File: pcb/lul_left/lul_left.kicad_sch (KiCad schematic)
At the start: 83 parts, among them SW1 SW_Push, SW10 SW_Push, SW11 SW_Push, SW12 SW_Push, SW13 SW_Push, SW14 SW_Push, SW15 SW_Push, SW16 SW_Push, SW17 SW_Push, SW18 SW_Push, SW19 SW_Push, SW2 SW_Push, SW20 SW_Push, SW21 SW_Push, SW22 SW_Push, SW23 SW_Push, SW24 SW_Push, SW25 SW_Push, SW26 SW_Push, SW27 SW_Push, SW28 SW_Push, SW29 SW_Push, SW3 SW_Push, SW30 SW_Push, SW31 SW_Push, SW32 SW_Push, SW33 SW_Push, SW34 SW_Push, SW35 SW_Push, SW36 SW_Push, SW37 SW_Push, SW38 SW_Push, SW39 SW_Push, SW4 SW_Push, SW40 SW_Push, SW41 SW_RESET, SW42 SW_SPDT, SW5 SW_Push, SW6 SW_Push, SW7 SW_Push, SW8 SW_Push, SW9 SW_Push, U2 nice_nano

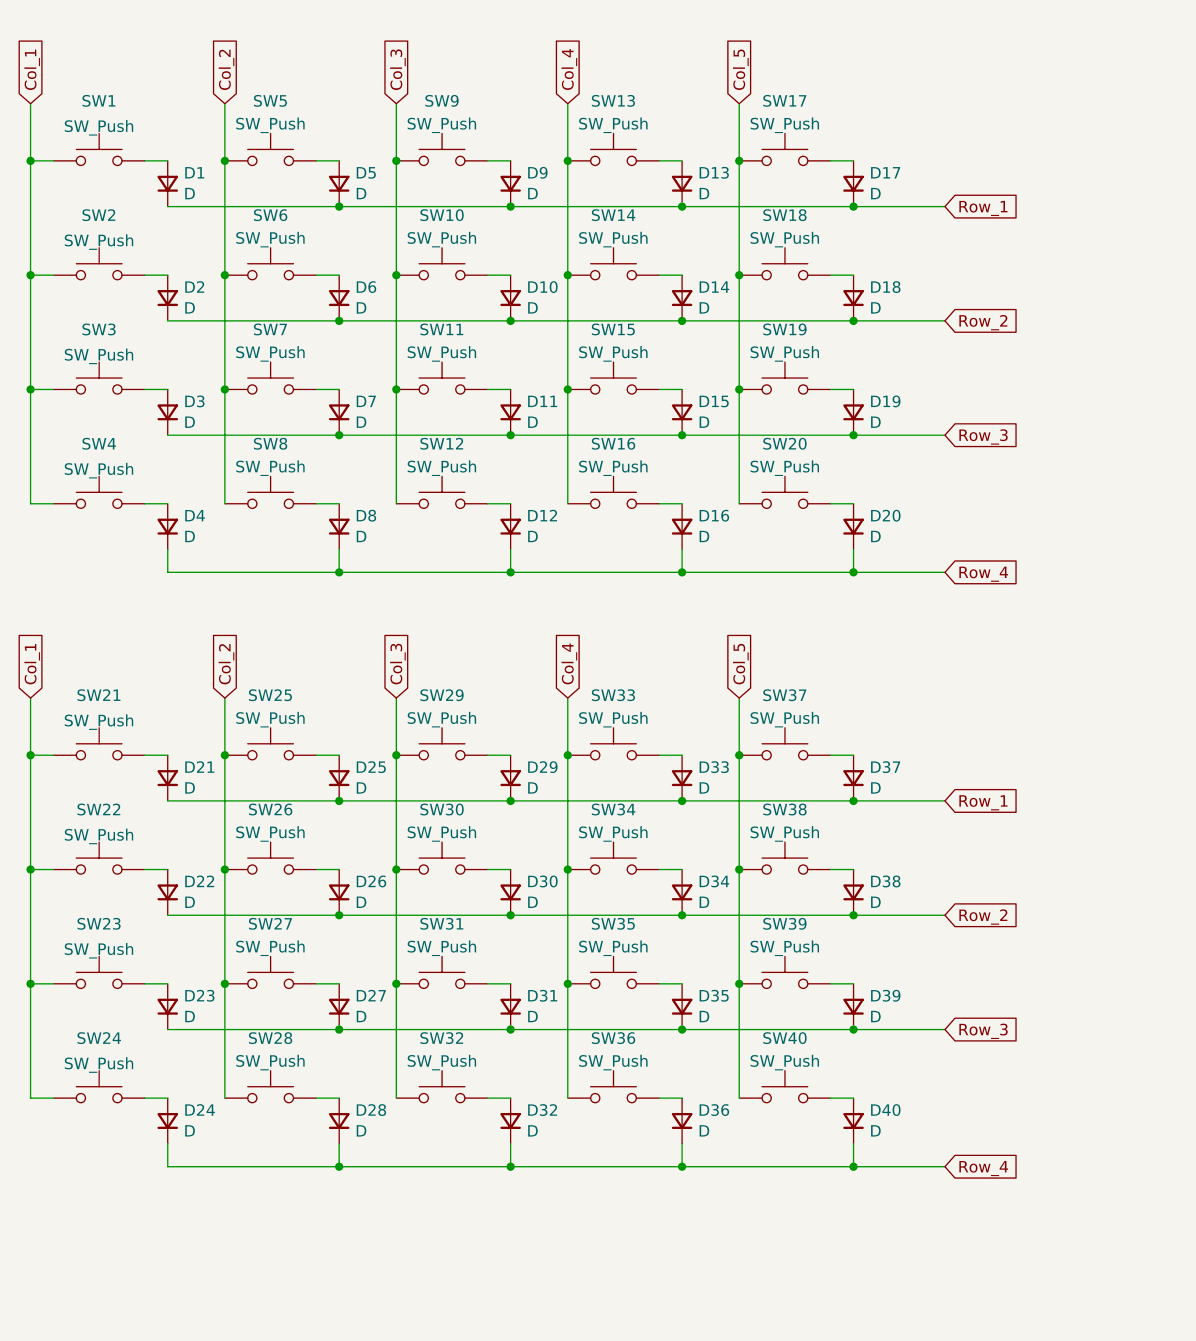
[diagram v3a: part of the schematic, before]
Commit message: Fixed switch count
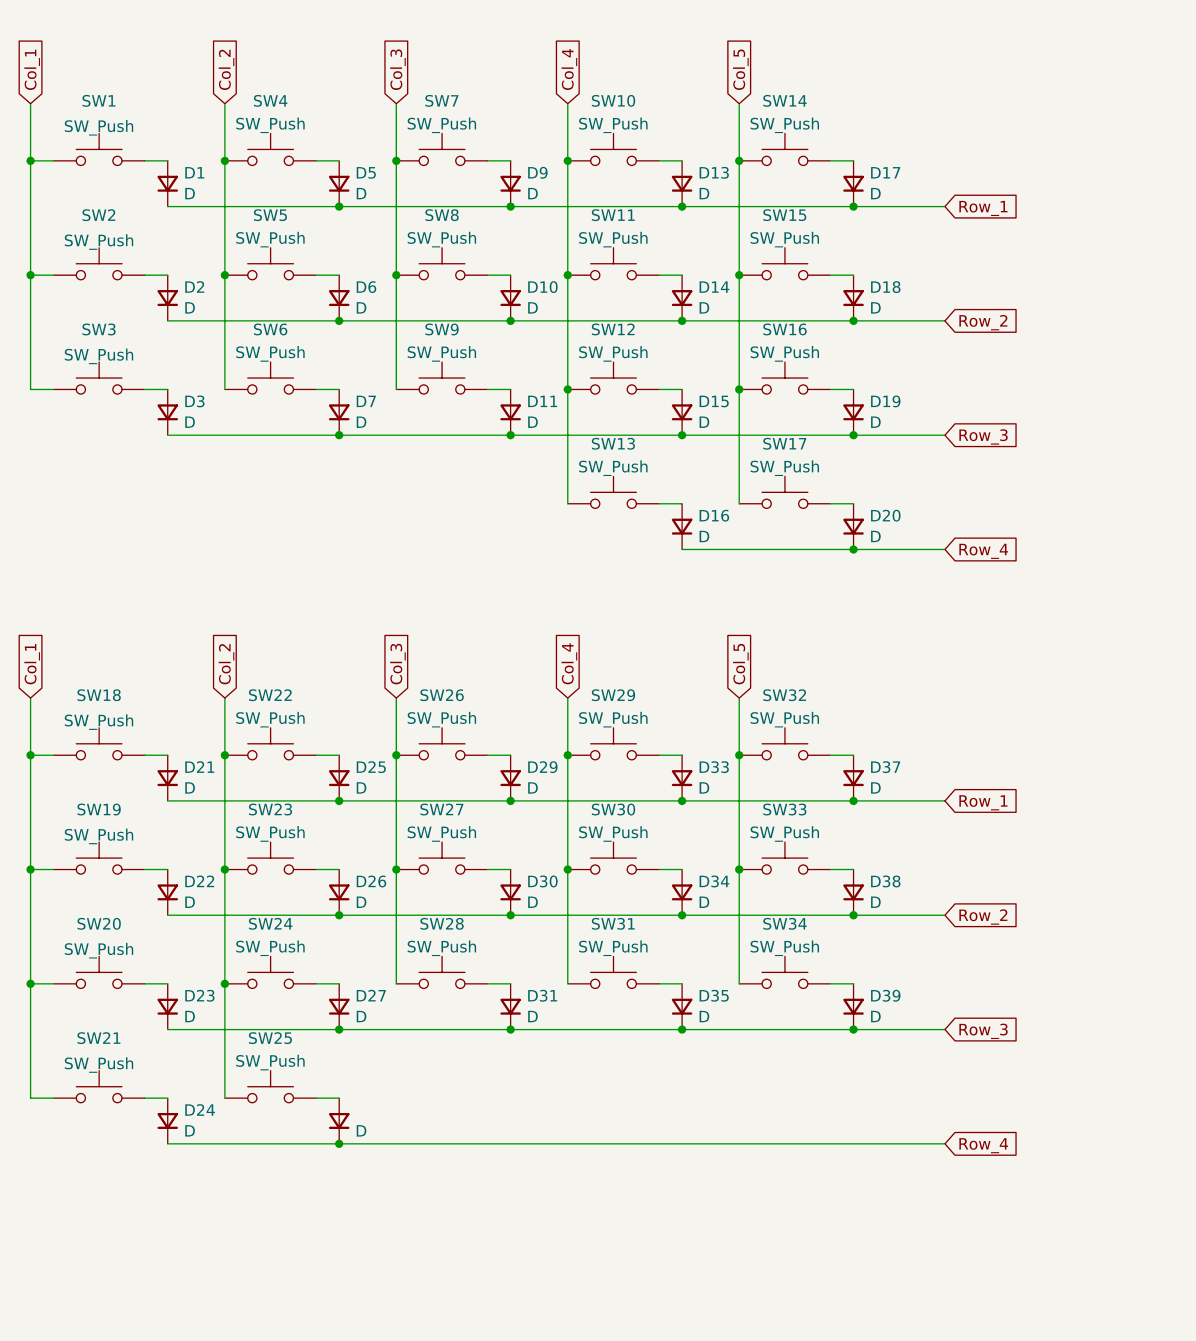
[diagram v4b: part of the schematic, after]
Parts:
- removed D12, D32, D36, D4, D40, D8: D, Diode_SMD:D_SOD-123, symbol Device:D_Small
- removed SW12, SW32, SW36, SW4, SW40, SW8: SW_Push, zzkeeb:Switch_MX-hotswap, symbol Switch:SW_Push
- renumbered SW13 to SW10, SW14 to SW11, SW15 to SW12, SW16 to SW13, SW17 to SW14, SW18 to SW15, SW19 to SW16, SW20 to SW17, SW21 to SW18, SW22 to SW19, SW23 to SW20, SW24 to SW21, SW25 to SW22, SW26 to SW23, SW27 to SW24, SW28 to SW25, SW29 to SW26, SW30 to SW27, SW31 to SW28, SW33 to SW29, SW34 to SW30, SW35 to SW31, SW37 to SW32, SW38 to SW33, SW39 to SW34, SW5 to SW4, SW6 to SW5, SW7 to SW6, SW9 to SW7, SW10 to SW8, SW11 to SW9

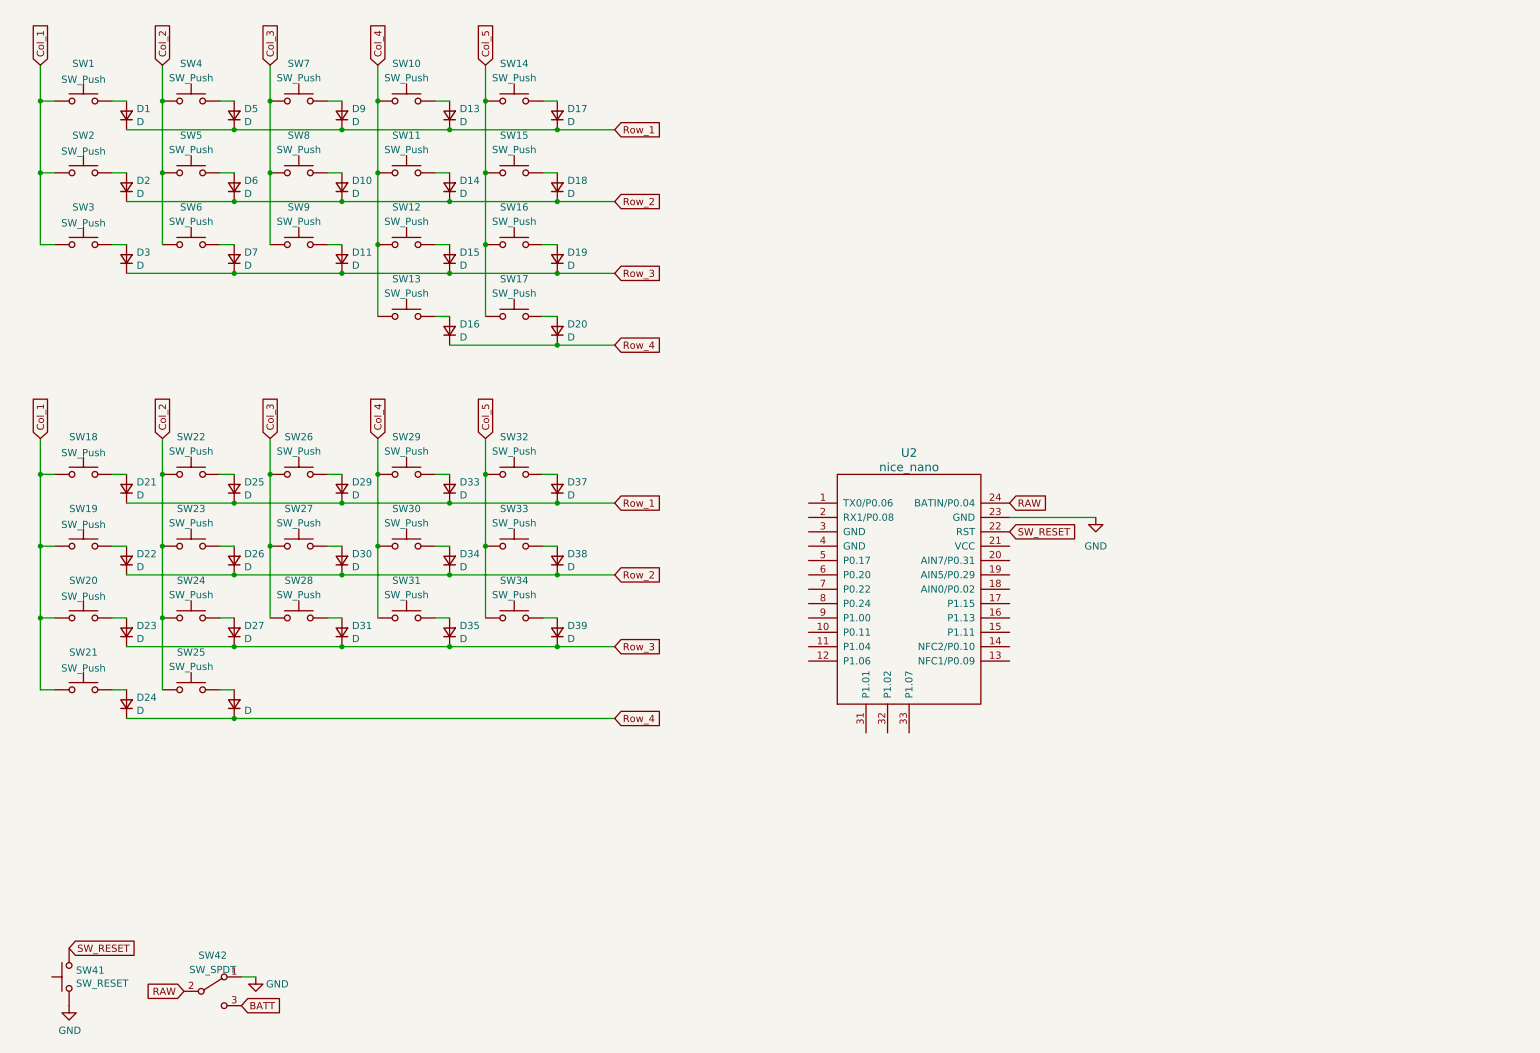
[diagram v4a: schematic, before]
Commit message: add controllers for both keyswitch matrices
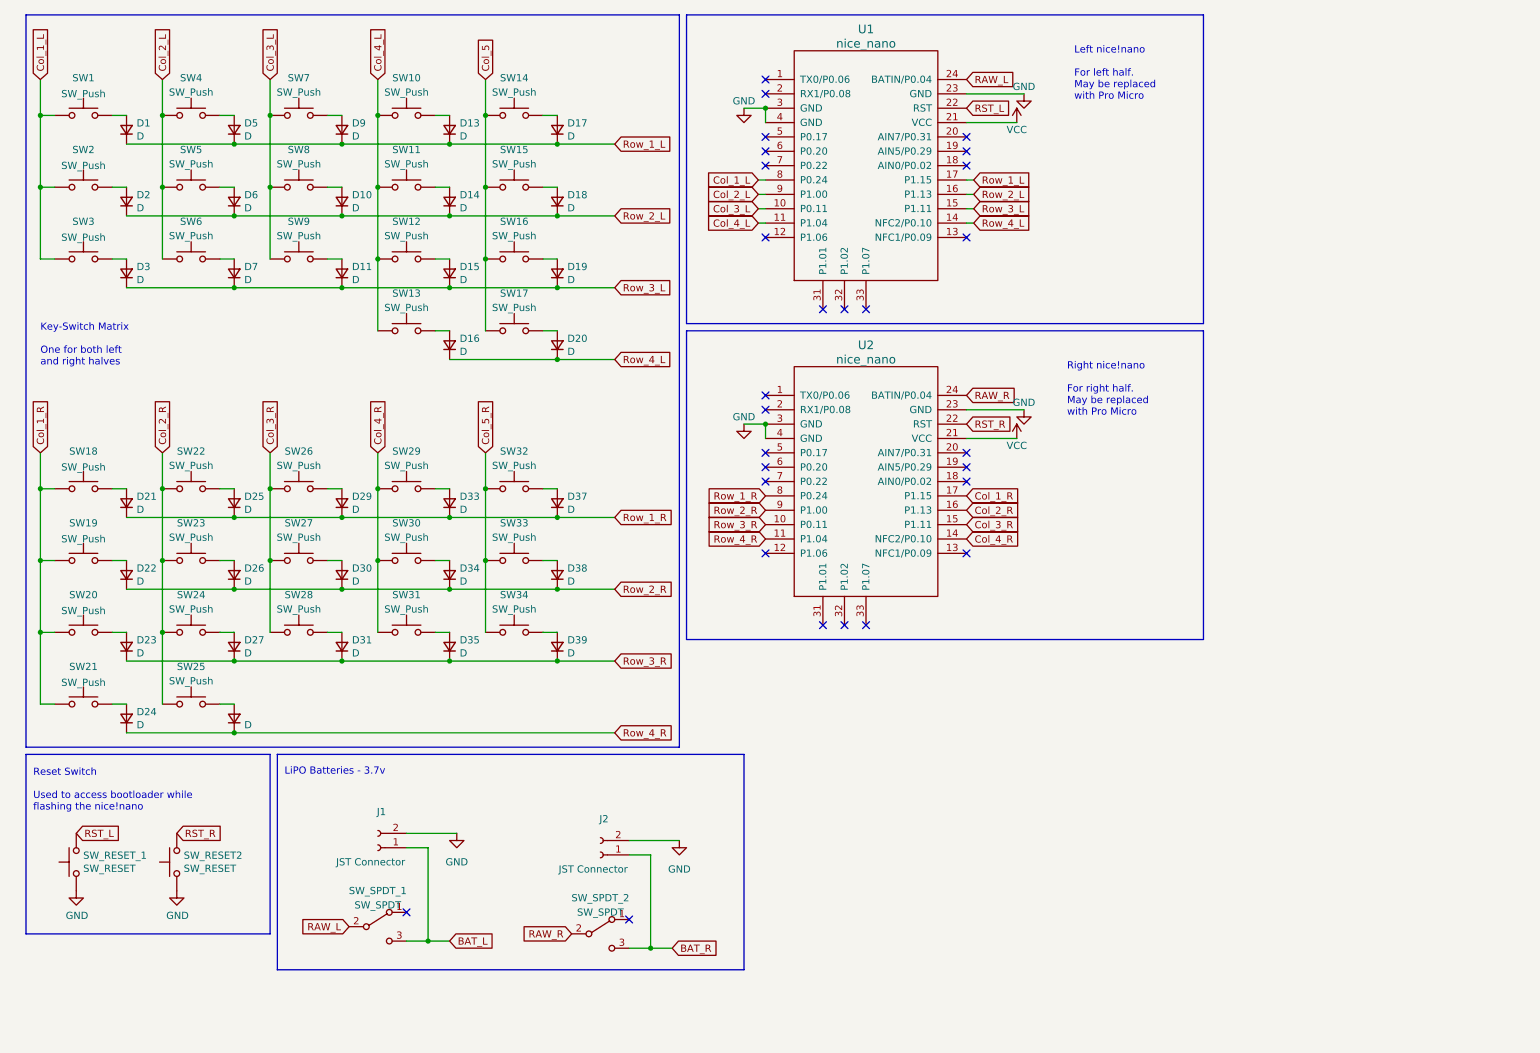
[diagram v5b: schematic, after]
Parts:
- added J1, J2: JST Connector, symbol Connector:Conn_01x02_Socket
- added SW_RESET2: SW_RESET, random-keyboard-parts:SKQG-1155865, symbol Switch:SW_Push
- added SW_SPDT_2: SW_SPDT, Button_Switch_SMD:SW_SPDT_PCM12, symbol Switch:SW_SPDT
- added U2: nice_nano, nice-nano-kicad:nice_nano, symbol nice_nano:nice_nano
- SW_SPDT_1: renamed from SW42; footprint (none) -> Button_Switch_SMD:SW_SPDT_PCM12
- U1: renamed from U2; footprint (none) -> nice-nano-kicad:nice_nano
- renumbered SW41 to SW_RESET_1
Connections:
- net Col_5: no longer SW32.1, SW33.1, SW34.1
- net GND: now also U1.3 (GND), U1.4 (GND), J1.2 (Pin_2), J2.2 (Pin_2), SW_RESET2.1, U2.23 (GND), U2.3 (GND), U2.4 (GND); no longer SW_SPDT_1.1 (A)
- net Col_3_L: now reaches U1.10 (P0.11)
- net Col_3_L: now also SW7.1, SW8.1, SW9.1
- net Col_4_L: now reaches U1.11 (P1.04)
- net Col_4_L: now also SW10.1, SW11.1, SW12.1, SW13.1
- net Row_4_L: now reaches U1.14 (NFC2/P0.10)
- net Row_4_L: now also D16.1 (K), D20.1 (K)
- net Row_3_L: now reaches U1.15 (P1.11)
- net Row_3_L: now also D11.1 (K), D15.1 (K), D19.1 (K), D3.1 (K), D7.1 (K)
- net Row_2_L: now reaches U1.16 (P1.13)
- net Row_2_L: now also D10.1 (K), D14.1 (K), D18.1 (K), D2.1 (K), D6.1 (K)
- net Row_1_L: now reaches U1.17 (P1.15)
- net Row_1_L: now also D1.1 (K), D13.1 (K), D17.1 (K), D5.1 (K), D9.1 (K)
- net VCC: now reaches U1.21 (VCC)
- net VCC: now also U2.21 (VCC)
- net Col_1_L: now reaches U1.8 (P0.24)
- net Col_1_L: now also SW1.1, SW2.1, SW3.1
- net Col_2_L: now reaches U1.9 (P1.00)
- net Col_2_L: now also SW4.1, SW5.1, SW6.1
- net BATT renamed BAT_L
- net BAT_L: now also J1.1 (Pin_1)
- net Col_1 renamed Col_1_R
- net Col_1_R: now also U2.17 (P1.15); no longer SW1.1, SW2.1, SW3.1
- net Col_2 renamed Col_2_R
- net Col_2_R: now also U2.16 (P1.13); no longer SW4.1, SW5.1, SW6.1
- net Col_3 renamed Col_3_R
- net Col_3_R: now also U2.15 (P1.11); no longer SW7.1, SW8.1, SW9.1
- removed net Col_4: SW10.1, SW11.1, SW12.1, SW13.1, SW29.1, SW30.1, SW31.1
- net RAW renamed RAW_L
- net Row_1 renamed Row_1_R
- net Row_1_R: now also U2.8 (P0.24); no longer D1.1 (K), D13.1 (K), D17.1 (K), D5.1 (K), D9.1 (K)
- net Row_2 renamed Row_2_R
- net Row_2_R: now also U2.9 (P1.00); no longer D10.1 (K), D14.1 (K), D18.1 (K), D2.1 (K), D6.1 (K)
- net Row_3 renamed Row_3_R
- net Row_3_R: now also U2.10 (P0.11); no longer D11.1 (K), D15.1 (K), D19.1 (K), D3.1 (K), D7.1 (K)
- net Row_4 renamed Row_4_R
- net Row_4_R: now also U2.11 (P1.04); no longer D16.1 (K), D20.1 (K)
- net SW_RESET renamed RST_L
- new net BAT_R: J2.1 (Pin_1), SW_SPDT_2.3 (C)
- new net Col_4_R: SW29.1, SW30.1, SW31.1, U2.14 (NFC2/P0.10)
- new net Col_5_R: SW32.1, SW33.1, SW34.1
- new net RAW_R: SW_SPDT_2.2 (B), U2.24 (BATIN/P0.04)
- new net RST_R: SW_RESET2.2, U2.22 (RST)
- no-connect marks 0 -> 28
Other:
- note added: "Key-Switch Matrix One for both left and right halves"
- note added: "Left nice!nano For left half. May be replaced with Pro Micro"
- note added: "LiPO Batteries - 3.7v"
- note added: "Reset Switch Used to access bootloader while flashing the nice!nano"
- note added: "Right nice!nano For right half. May be replaced with Pro Micro"
- moved on the sheet: D1, D10, D11, D13, D14, D15, D16, D17, D18, D19, D2, D20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
